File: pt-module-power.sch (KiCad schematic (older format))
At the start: 19 parts

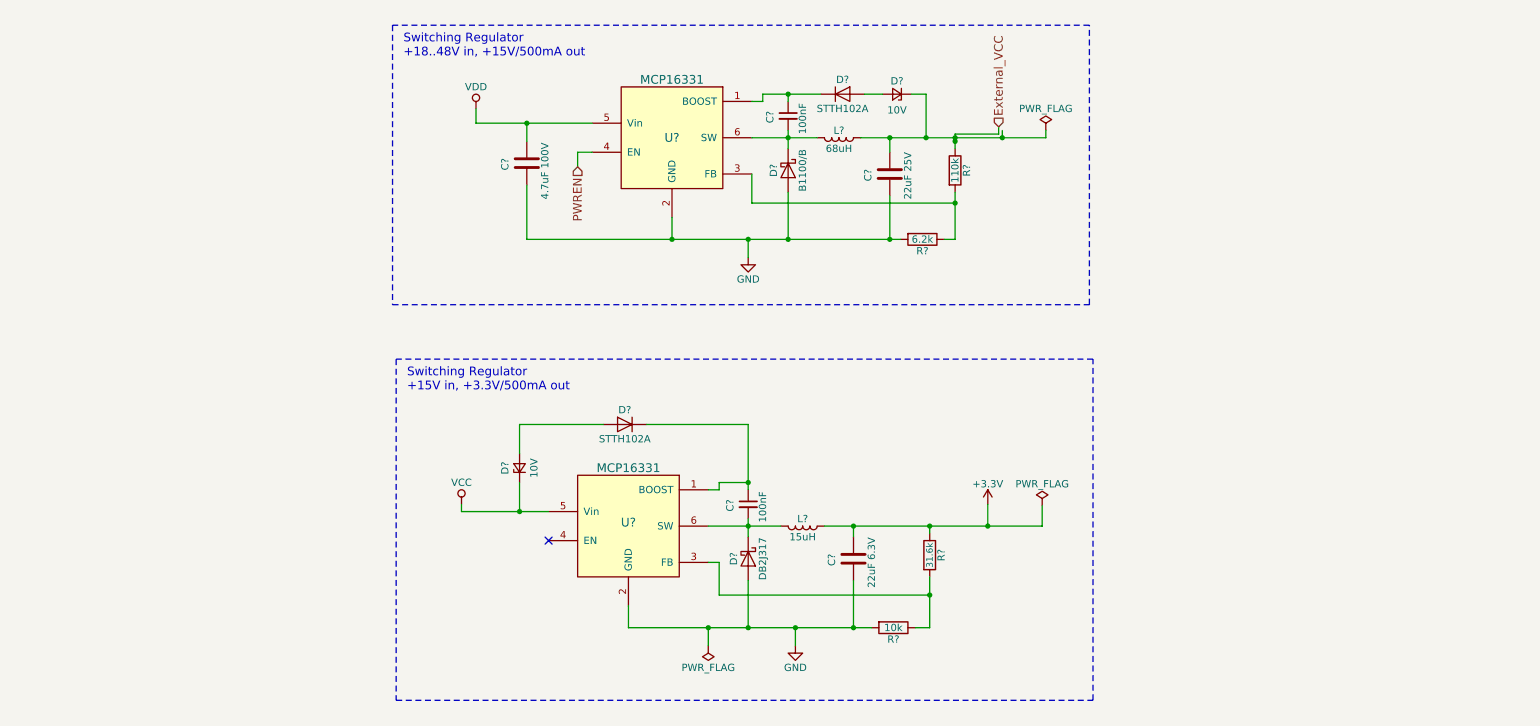
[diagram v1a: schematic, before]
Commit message: add regulator suggestion
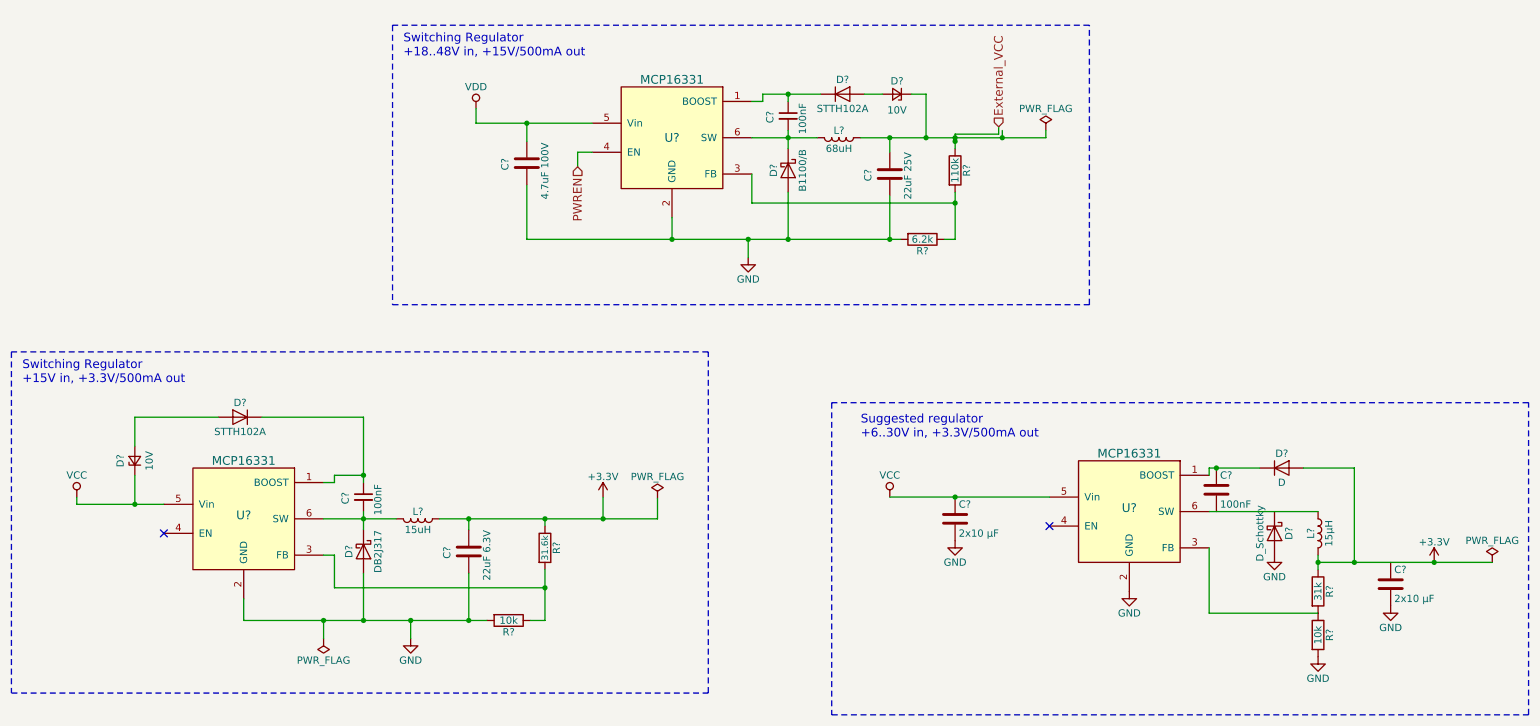
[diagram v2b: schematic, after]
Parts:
- added C? (x2): 2x10 µF, symbol C
- added C?: 100nF, symbol C
- added D?: D_Schottky, symbol D_Schottky
- added D?: D, symbol D
- added L?: 15µH, symbol L
- added R?: 10k, symbol R
- added R?: 31k, symbol R
- added U?: MCP16331, TO_SOT_Packages_SMD:SOT-23-6, symbol MCP16331
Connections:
- net +3V3: now also D?.2 (A), L?.2, R?.1
- net GND: now also C?.2, C?.2, D?.2 (A), R?.2, U?.2 (GND)
- net VCC: now also C?.1, U?.5 (Vin)
- new net: C?.1, D?.1 (K), U?.1 (BOOST)
- new net: R?.1, R?.2, U?.3 (FB)
- new net: L?.1, U?.6 (SW)
- no-connect marks 1 -> 2
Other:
- note added: "Suggested regulator\n+6..30V in, +3.3V/500mA out"
- moved on the sheet: C?, D?, L?, R?, U?

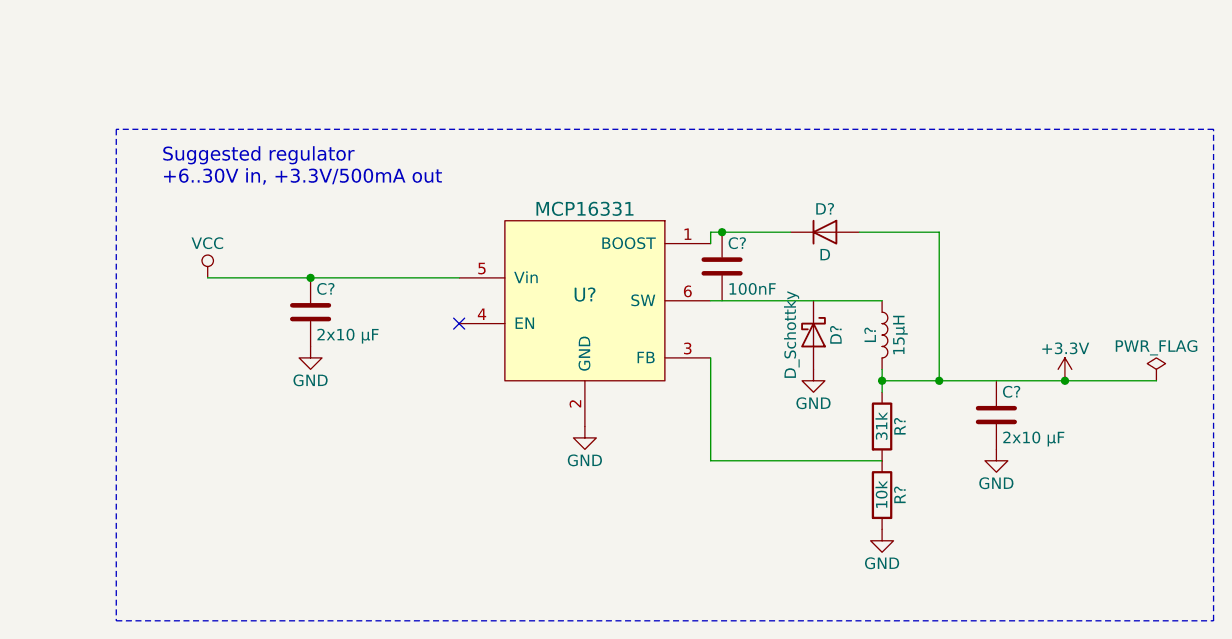
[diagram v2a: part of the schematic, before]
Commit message: add capacitor values
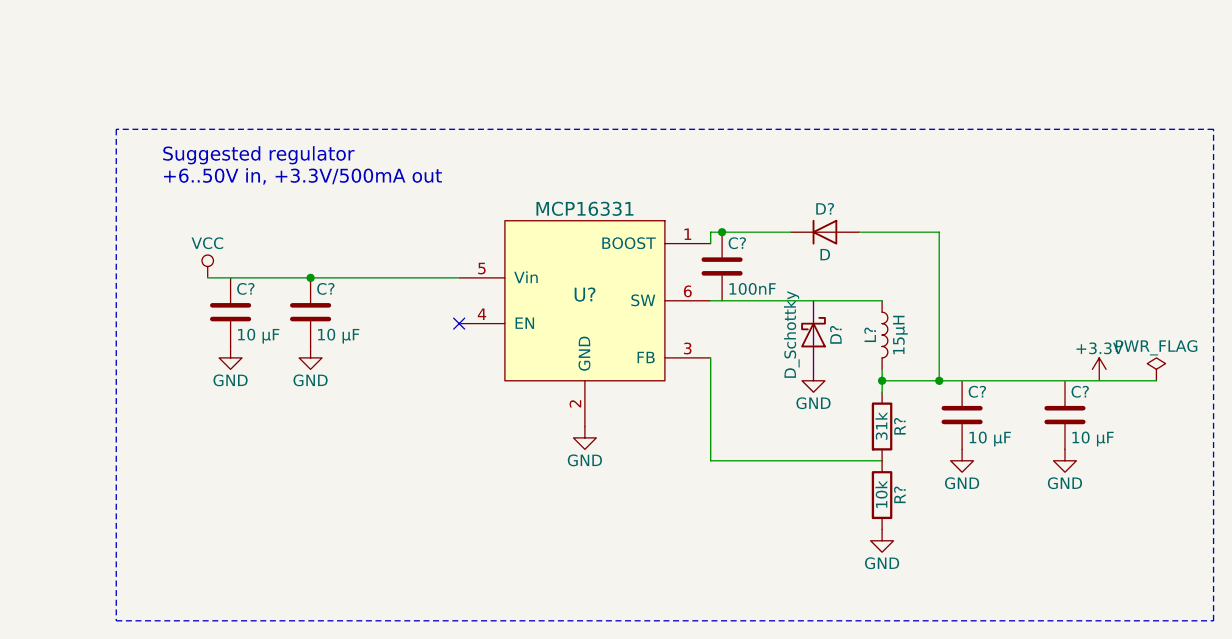
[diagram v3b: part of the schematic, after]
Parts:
- added C? (x2): 10 µF, symbol C
- C? (x2): value 2x10 µF -> 10 µF
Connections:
- net +3V3: no longer D?.2 (A), L?.2, R?.1
- net GND: now also C?.2, C?.2
- new net: D?.2 (A), L?.2, R?.1
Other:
- note added: "Suggested regulator\n+6..50V in, +3.3V/500mA out"
- note removed: "Suggested regulator\n+6..30V in, +3.3V/500mA out"
- moved on the sheet: C?
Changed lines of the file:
@@
 P 7100 4900
 F 0 "C?" H 7125 5000 50  0000 L CNN
-F 1 "2x10 µF" H 7125 4800 50  0000 L CNN
+F 1 "10 µF" H 7125 4800 50  0000 L CNN
 F 2 "" H 7138 4750 50  0001 C CNN
 F 3 "" H 7100 4900 50  0001 C CNN
@@
 L +3.3V #PWR?
 U 1 1 598C94DC
-P 10400 5200
-F 0 "#PWR?" H 10400 5050 50  0001 C CNN
-F 1 "+3.3V" H 10400 5340 50  0000 C CNN
-F 2 "" H 10400 5200 50  0001 C CNN
-F 3 "" H 10400 5200 50  0001 C CNN
-	1    10400 5200
+P 10550 5200
+F 0 "#PWR?" H 10550 5050 50  0001 C CNN
+F 1 "+3.3V" H 10550 5340 50  0000 C CNN
+F 2 "" H 10550 5200 50  0001 C CNN
+F 3 "" H 10550 5200 50  0001 C CNN
+	1    10550 5200
 	1    0    0    -1
 $EndComp
@@
 	1    0    0    -1
 $EndComp
-Connection ~ 10400 5200
 $Comp
 L GND #PWR?
 U 1 1 598CA371
-P 10100 5500
-F 0 "#PWR?" H 10100 5250 50  0001 C CNN
-F 1 "GND" H 10100 5350 50  0000 C CNN
-F 2 "" H 10100 5500 50  0001 C CNN
-F 3 "" H 10100 5500 50  0001 C CNN
-	1    10100 5500
+P 9950 5500
+F 0 "#PWR?" H 9950 5250 50  0001 C CNN
+F 1 "GND" H 9950 5350 50  0000 C CNN
+F 2 "" H 9950 5500 50  0001 C CNN
+F 3 "" H 9950 5500 50  0001 C CNN
+	1    9950 5500
 	1    0    0    -1
 $EndComp
@@
 	11050 4100 6250 4100
 Text Notes 6450 4350 0    60   ~ 0
-Suggested regulator\n+6..30V in, +3.3V/500mA out
+Suggested regulator\n+6..50V in, +3.3V/500mA out
 $Comp
 L C C?
 U 1 1 598C8ED1
-P 10100 5350
-F 0 "C?" H 10125 5450 50  0000 L CNN
-F 1 "2x10 µF" H 10125 5250 50  0000 L CNN
-F 2 "" H 10138 5200 50  0001 C CNN
-F 3 "" H 10100 5350 50  0001 C CNN
-	1    10100 5350
-	1    0    0    -1
-$EndComp
+P 9950 5350
+F 0 "C?" H 9975 5450 50  0000 L CNN
+F 1 "10 µF" H 9975 5250 50  0000 L CNN
+F 2 "" H 9988 5200 50  0001 C CNN
+F 3 "" H 9950 5350 50  0001 C CNN
+	1    9950 5350
+	1    0    0    -1
+$EndComp
+$Comp
+L C C?
+U 1 1 598CEAC9
+P 6750 4900
+F 0 "C?" H 6775 5000 50  0000 L CNN
+F 1 "10 µF" H 6775 4800 50  0000 L CNN
+F 2 "" H 6788 4750 50  0001 C CNN
+F 3 "" H 6750 4900 50  0001 C CNN
+	1    6750 4900
+	1    0    0    -1
+$EndComp
+$Comp
+L GND #PWR?
+U 1 1 598CEACF
+P 6750 5050
+F 0 "#PWR?" H 6750 4800 50  0001 C CNN
+F 1 "GND" H 6750 4900 50  0000 C CNN
+F 2 "" H 6750 5050 50  0001 C CNN
+F 3 "" H 6750 5050 50  0001 C CNN
+	1    6750 5050
+	1    0    0    -1
+$EndComp
+$Comp
+L GND #PWR?
+U 1 1 598CEF8A
+P 10400 5500
+F 0 "#PWR?" H 10400 5250 50  0001 C CNN
+F 1 "GND" H 10400 5350 50  0000 C CNN
+F 2 "" H 10400 5500 50  0001 C CNN
+F 3 "" H 10400 5500 50  0001 C CNN
+	1    10400 5500
+	1    0    0    -1
+$EndComp
+$Comp
+L C C?
+U 1 1 598CEF90
+P 10400 5350
+F 0 "C?" H 10425 5450 50  0000 L CNN
+F 1 "10 µF" H 10425 5250 50  0000 L CNN
+F 2 "" H 10438 5200 50  0001 C CNN
+F 3 "" H 10400 5350 50  0001 C CNN
+	1    10400 5350
+	1    0    0    -1
+$EndComp

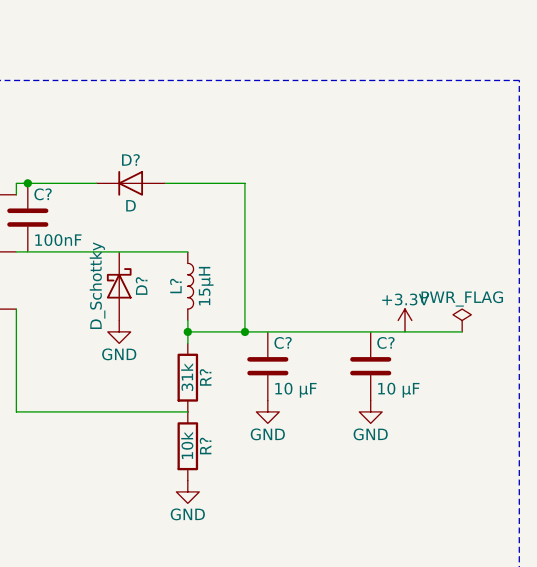
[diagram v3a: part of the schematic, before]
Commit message: indeces to interfacemodules
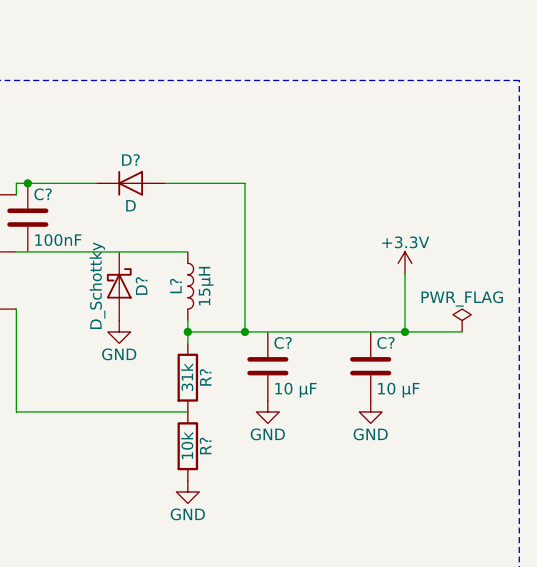
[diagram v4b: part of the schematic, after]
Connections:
- net +3V3: now also D?.2 (A), L?.2, R?.1
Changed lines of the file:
@@
 Text HLabel 7400 2200 1    60   Input ~ 0
 External_VCC
-Wire Wire Line
-	7100 2275 7100 2350
-Connection ~ 7100 2275
-Wire Wire Line
-	7425 2275 7425 2225
-Wire Wire Line
-	5700 2725 5700 2525
-Connection ~ 6900 2275
-Wire Wire Line
-	6900 1975 6800 1975
-Wire Wire Line
-	6900 2275 6900 1975
-Wire Wire Line
-	6475 1975 6600 1975
-Wire Wire Line
-	6450 2275 7725 2275
-Wire Wire Line
-	5775 1975 6175 1975
-Wire Wire Line
-	5950 2225 5950 2350
-Wire Wire Line
-	5700 2275 6150 2275
-Wire Wire Line
-	4150 2600 4150 2975
-Wire Wire Line
-	3800 2075 3800 2175
-Wire Wire Line
-	5950 2975 5950 2650
-Connection ~ 5950 2975
-Wire Wire Line
-	1050 4750 1050 4800
-Wire Wire Line
-	1050 4800 1650 4800
-Wire Wire Line
-	1450 4800 1450 4600
-Connection ~ 1450 4800
-Wire Wire Line
-	1450 4400 1450 4200
-Wire Wire Line
-	1450 4200 2025 4200
-Wire Wire Line
-	2750 4900 3250 4900
-Wire Wire Line
-	3550 4900 5050 4900
-Wire Wire Line
-	3025 4850 3025 4975
-Wire Wire Line
-	3025 4200 3025 4650
-Wire Wire Line
-	2325 4200 3025 4200
-Connection ~ 6650 2975
-Wire Wire Line
-	3750 4900 3750 4975
-Connection ~ 3025 4900
-Wire Wire Line
-	4275 4900 4275 4950
-Connection ~ 3750 4900
-Wire Wire Line
-	2750 5150 2825 5150
-Wire Wire Line
-	2825 5150 2825 5375
-Wire Wire Line
-	2825 5375 4275 5375
-Wire Wire Line
-	4275 5250 4275 5600
-Connection ~ 4275 5375
-Wire Wire Line
-	2200 5600 3875 5600
-Wire Wire Line
-	3025 5275 3025 5600
-Connection ~ 3025 5600
-Wire Wire Line
-	3750 5600 3750 5275
-Connection ~ 3750 5600
-Wire Wire Line
-	4675 4900 4675 4750
-Connection ~ 4275 4900
-Wire Wire Line
-	6650 2275 6650 2375
-Connection ~ 6650 2275
-Wire Wire Line
-	3800 2175 4600 2175
-Wire Wire Line
-	4150 2175 4150 2300
-Connection ~ 4150 2175
-Connection ~ 5950 2275
-Wire Wire Line
-	5950 1975 5950 2025
-Connection ~ 5950 1975
-Wire Wire Line
-	5775 1975 5775 2025
-Wire Wire Line
-	5775 2025 5700 2025
-Wire Wire Line
-	3025 4600 2825 4600
-Wire Wire Line
-	2825 4600 2825 4650
-Wire Wire Line
-	2825 4650 2750 4650
-Connection ~ 3025 4600
-Wire Wire Line
-	4275 5600 4175 5600
-Wire Wire Line
-	2200 5450 2200 5600
-Wire Wire Line
-	3350 5600 3350 5725
-Connection ~ 3350 5600
-Wire Wire Line
-	6650 2975 6650 2675
-Wire Wire Line
-	7100 2975 7025 2975
-Wire Wire Line
-	4150 2975 6725 2975
-Wire Wire Line
-	5675 2975 5675 3100
-Connection ~ 5675 2975
-Wire Wire Line
-	5150 2825 5150 2975
-Connection ~ 5150 2975
-Wire Wire Line
-	5700 2725 7100 2725
-Connection ~ 7100 2725
-Wire Notes Line
-	3225 1500 3225 3425
-Wire Notes Line
-	3225 3425 8025 3425
-Wire Notes Line
-	8025 3425 8025 1500
-Wire Notes Line
-	8025 1500 3225 1500
-Wire Notes Line
-	600  3750 600  6100
-Wire Notes Line
-	600  6100 5400 6100
-Wire Notes Line
-	5400 6100 5400 3750
-Wire Notes Line
-	5400 3750 600  3750
-Wire Wire Line
-	7725 2275 7725 2225
-Connection ~ 7425 2275
-Wire Wire Line
-	5050 4900 5050 4760
-Connection ~ 4675 4900
-Wire Wire Line
-	4500 2475 4500 2375
-Wire Wire Line
-	4500 2375 4600 2375
-Wire Wire Line
-	2750 5600 2750 5725
-Connection ~ 2750 5600
-Wire Wire Line
-	7100 2650 7100 2975
-Wire Wire Line
-	7400 2200 7400 2250
-Wire Wire Line
-	7400 2250 7100 2250
-Wire Wire Line
-	7100 2250 7100 2300
-Connection ~ 7100 2300
 $Comp
 L MCP16331 U?
@@
 	1    0    0    -1
 $EndComp
-Wire Wire Line
-	6650 4750 7750 4750
-Connection ~ 7100 4750
 $Comp
 L GND #PWR?
@@
 	1    0    0    -1
 $EndComp
-Wire Wire Line
-	8850 5550 9600 5550
-Wire Wire Line
-	8850 4850 9600 4850
 $Comp
 L L L?
@@
 	1    0    0    -1
 $EndComp
-Wire Wire Line
-	8850 5550 8850 5100
-Wire Wire Line
-	9600 5250 9600 5150
-Connection ~ 9600 5200
-Connection ~ 9850 5200
 $Comp
 L C C?
@@
 	1    0    0    -1
 $EndComp
-Wire Wire Line
-	8850 4600 8850 4550
-Wire Wire Line
-	8850 4550 9200 4550
-Connection ~ 8900 4550
 $Comp
 L D D?
@@
 	1    0    0    -1
 $EndComp
-Wire Wire Line
-	9500 4550 9850 4550
-Wire Wire Line
-	9850 4550 9850 5200
-Wire Wire Line
-	9600 5200 10800 5200
 $Comp
 L +3.3V #PWR?
 U 1 1 598C94DC
-P 10550 5200
-F 0 "#PWR?" H 10550 5050 50  0001 C CNN
-F 1 "+3.3V" H 10550 5340 50  0000 C CNN
-F 2 "" H 10550 5200 50  0001 C CNN
-F 3 "" H 10550 5200 50  0001 C CNN
-	1    10550 5200
+P 10550 4950
+F 0 "#PWR?" H 10550 4800 50  0001 C CNN
+F 1 "+3.3V" H 10550 5090 50  0000 C CNN
+F 2 "" H 10550 4950 50  0001 C CNN
+F 3 "" H 10550 4950 50  0001 C CNN
+	1    10550 4950
 	1    0    0    -1
 $EndComp
@@
 	1    0    0    -1
 $EndComp
-Wire Notes Line
-	6250 4100 6250 6250
-Wire Notes Line
-	6250 6250 11050 6250
-Wire Notes Line
-	11050 6250 11050 4100
-Wire Notes Line
-	11050 4100 6250 4100
 Text Notes 6450 4350 0    60   ~ 0
 Suggested regulator\n+6..50V in, +3.3V/500mA out
@@
 	1    0    0    -1
 $EndComp
+Wire Wire Line
+	7100 2275 7100 2350
+Connection ~ 7100 2275
+Wire Wire Line
+	7425 2275 7425 2225
+Wire Wire Line
+	5700 2725 5700 2525
+Connection ~ 6900 2275
+Wire Wire Line
+	6900 1975 6800 1975
+Wire Wire Line
+	6900 2275 6900 1975
+Wire Wire Line
+	6475 1975 6600 1975
+Wire Wire Line
+	6450 2275 7725 2275
+Wire Wire Line
+	5775 1975 6175 1975
+Wire Wire Line
+	5950 2225 5950 2350
+Wire Wire Line
+	5700 2275 6150 2275
+Wire Wire Line
+	4150 2600 4150 2975
+Wire Wire Line
+	3800 2075 3800 2175
+Wire Wire Line
+	5950 2975 5950 2650
+Connection ~ 5950 2975
+Wire Wire Line
+	1050 4750 1050 4800
+Wire Wire Line
+	1050 4800 1650 4800
+Wire Wire Line
+	1450 4800 1450 4600
+Connection ~ 1450 4800
+Wire Wire Line
+	1450 4400 1450 4200
+Wire Wire Line
+	1450 4200 2025 4200
+Wire Wire Line
+	2750 4900 3250 4900
+Wire Wire Line
+	3550 4900 5050 4900
+Wire Wire Line
+	3025 4850 3025 4975
+Wire Wire Line
+	3025 4200 3025 4650
+Wire Wire Line
+	2325 4200 3025 4200
+Connection ~ 6650 2975
+Wire Wire Line
+	3750 4900 3750 4975
+Connection ~ 3025 4900
+Wire Wire Line
+	4275 4900 4275 4950
+Connection ~ 3750 4900
+Wire Wire Line
+	2750 5150 2825 5150
+Wire Wire Line
+	2825 5150 2825 5375
+Wire Wire Line
+	2825 5375 4275 5375
+Wire Wire Line
+	4275 5250 4275 5600
+Connection ~ 4275 5375
+Wire Wire Line
+	2200 5600 3875 5600
+Wire Wire Line
+	3025 5275 3025 5600
+Connection ~ 3025 5600
+Wire Wire Line
+	3750 5600 3750 5275
+Connection ~ 3750 5600
+Wire Wire Line
+	4675 4900 4675 4750
+Connection ~ 4275 4900
+Wire Wire Line
+	6650 2275 6650 2375
+Connection ~ 6650 2275
+Wire Wire Line
+	3800 2175 4600 2175
+Wire Wire Line
+	4150 2175 4150 2300
+Connection ~ 4150 2175
+Connection ~ 5950 2275
+Wire Wire Line
+	5950 1975 5950 2025
+Connection ~ 5950 1975
+Wire Wire Line
+	5775 1975 5775 2025
+Wire Wire Line
+	5775 2025 5700 2025
+Wire Wire Line
+	3025 4600 2825 4600
+Wire Wire Line
+	2825 4600 2825 4650
+Wire Wire Line
+	2825 4650 2750 4650
+Connection ~ 3025 4600
+Wire Wire Line
+	4275 5600 4175 5600
+Wire Wire Line
+	2200 5450 2200 5600
+Wire Wire Line
+	3350 5600 3350 5725
+Connection ~ 3350 5600
+Wire Wire Line
+	6650 2975 6650 2675
+Wire Wire Line
+	7100 2975 7025 2975
+Wire Wire Line
+	4150 2975 6725 2975
+Wire Wire Line
+	5675 2975 5675 3100
+Connection ~ 5675 2975
+Wire Wire Line
+	5150 2825 5150 2975
+Connection ~ 5150 2975
+Wire Wire Line
+	5700 2725 7100 2725
+Connection ~ 7100 2725
+Wire Notes Line
+	3225 1500 3225 3425
+Wire Notes Line
+	3225 3425 8025 3425
+Wire Notes Line
+	8025 3425 8025 1500
+Wire Notes Line
+	8025 1500 3225 1500
+Wire Notes Line
+	600  3750 600  6100
+Wire Notes Line
+	600  6100 5400 6100
+Wire Notes Line
+	5400 6100 5400 3750
+Wire Notes Line
+	5400 3750 600  3750
+Wire Wire Line
+	7725 2275 7725 2225
+Connection ~ 7425 2275
+Wire Wire Line
+	5050 4900 5050 4760
+Connection ~ 4675 4900
+Wire Wire Line
+	4500 2475 4500 2375
+Wire Wire Line
+	4500 2375 4600 2375
+Wire Wire Line
+	2750 5600 2750 5725
+Connection ~ 2750 5600
+Wire Wire Line
+	7100 2650 7100 2975
+Wire Wire Line
+	7400 2200 7400 2250
+Wire Wire Line
+	7400 2250 7100 2250
+Wire Wire Line
+	7100 2250 7100 2300
+Connection ~ 7100 2300
+Wire Wire Line
+	6650 4750 7750 4750
+Connection ~ 7100 4750
+Wire Wire Line
+	8850 5550 9600 5550
+Wire Wire Line
+	8850 4850 9600 4850
+Wire Wire Line
+	8850 5550 8850 5100
+Wire Wire Line
+	9600 5250 9600 5150
+Connection ~ 9600 5200
+Connection ~ 9850 5200
+Wire Wire Line
+	8850 4600 8850 4550
+Wire Wire Line
+	8850 4550 9200 4550
+Connection ~ 8900 4550
+Wire Wire Line
+	9500 4550 9850 4550
+Wire Wire Line
+	9850 4550 9850 5200
+Wire Wire Line
+	9600 5200 10800 5200
+Wire Notes Line
+	6250 4100 6250 6250
+Wire Notes Line
+	6250 6250 11050 6250
+Wire Notes Line
+	11050 6250 11050 4100
+Wire Notes Line
+	11050 4100 6250 4100
+Wire Wire Line
+	10550 4950 10550 5200
+Connection ~ 10550 5200
 $EndSCHEMATC
